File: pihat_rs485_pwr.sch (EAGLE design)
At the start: 36 parts, among them J1 RASPBERRYPI-40-PIN-GPIO_PTH_N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, Q1 MOSFET-N2N7002, Q2 MOSFET-N2N7002, Q3 MOSFET-N2N7002, Q4 MOSFET-P_SMD, Q5 BIPOLAR_TRANS_ARRAY, U1 MAX481CSA

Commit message: 11/29/17, changed PS, term blocks
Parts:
- 485: value TERMBLK_3PINNOSILK -> TERMBLK_3PINFEMALE; device UPenn:TERMBLK_3PINNOSILK -> UPenn:TERMBLK_3PINFEMALE
- PS1: value D24V22F5 -> R-78-E5.0; device UPenn:D24V22F5 -> UPenn:R-78-E5.0
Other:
- moved on the sheet: 485
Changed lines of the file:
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@@
 <part name="SUPPLY7" library="SparkFun-PowerSymbols" deviceset="3.3V" device=""/>
 <part name="SUPPLY9" library="SparkFun-PowerSymbols" deviceset="3.3V" device=""/>
-<part name="485" library="UPenn" deviceset="TERMBLK_3PIN" device="NOSILK"/>
+<part name="485" library="UPenn" deviceset="TERMBLK_3PIN" device="FEMALE" value="TERMBLK_3PINFEMALE"/>
 <part name="POWER" library="UPenn" deviceset="TERMBLK_3PIN" device="NOSILK"/>
 <part name="S1" library="UPenn" deviceset="DPDT_DIP_SMD" device=""/>
@@
 <part name="GND10" library="SparkFun-PowerSymbols" deviceset="GND" device=""/>
 <part name="GND12" library="SparkFun-PowerSymbols" deviceset="GND" device=""/>
-<part name="PS1" library="UPenn" deviceset="D24V22F5" device=""/>
+<part name="PS1" library="UPenn" deviceset="R-78-E5.0" device=""/>
 </parts>
 <sheets>
@@
 <instance part="GND10" gate="1" x="218.44" y="64.77"/>
 <instance part="GND12" gate="1" x="153.67" y="71.12"/>
-<instance part="PS1" gate="G$1" x="175.26" y="121.92"/>
+<instance part="PS1" gate="G$1" x="175.26" y="119.38"/>
 </instances>
 <busses>
@@
 <pinref part="SUPPLY2" gate="G$1" pin="VIN"/>
 <wire x1="160.02" y1="128.27" x2="165.1" y2="128.27" width="0.1524" layer="91"/>
+<wire x1="165.1" y1="121.92" x2="165.1" y2="128.27" width="0.1524" layer="91"/>
 <pinref part="PS1" gate="G$1" pin="VIN"/>
 <wire x1="167.64" y1="121.92" x2="165.1" y2="121.92" width="0.1524" layer="91"/>
-<wire x1="165.1" y1="121.92" x2="165.1" y2="128.27" width="0.1524" layer="91"/>
 </segment>
 </net>
@@
 <pinref part="GND2" gate="1" pin="GND"/>
 <wire x1="160.02" y1="123.19" x2="162.56" y2="123.19" width="0.1524" layer="91"/>
-<pinref part="PS1" gate="G$1" pin="GND"/>
 <wire x1="167.64" y1="119.38" x2="162.56" y2="119.38" width="0.1524" layer="91"/>
 <wire x1="162.56" y1="119.38" x2="162.56" y2="123.19" width="0.1524" layer="91"/>
+<pinref part="PS1" gate="G$1" pin="GND"/>
 </segment>
 <segment>

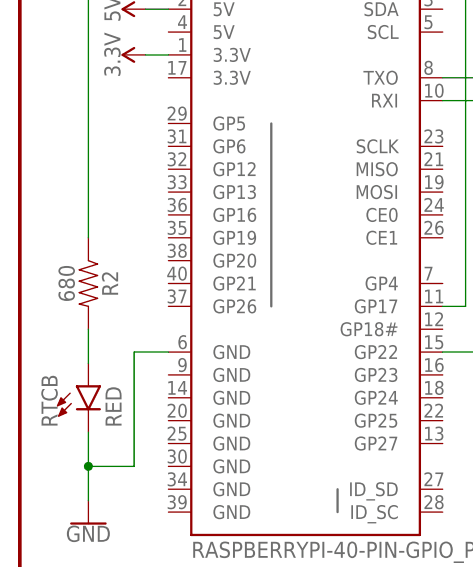
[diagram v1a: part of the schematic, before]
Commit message: 1/8/18, change R2 value from 680 to 510 to reduce parts
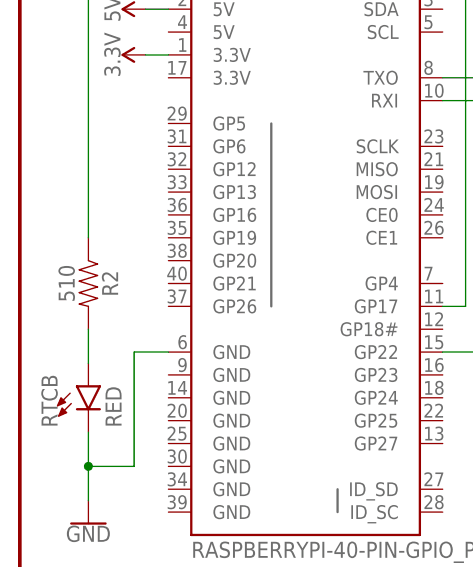
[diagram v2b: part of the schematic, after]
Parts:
- R2: value 680 -> 510
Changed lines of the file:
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@@
 <parts>
 <part name="FRAME1" library="SparkFun-Aesthetics" deviceset="FRAME-LETTER" device="NO_PACKAGE"/>
-<part name="R2" library="SparkFun-Resistors" deviceset="RESISTOR" device="0603" value="680"/>
+<part name="R2" library="SparkFun-Resistors" deviceset="RESISTOR" device="0603" value="510"/>
 <part name="R6" library="SparkFun-Resistors" deviceset="RESISTOR" device="0603" value="1K"/>
 <part name="PWR" library="SparkFun-LED" deviceset="LED" device="0603" value="GRN"/>
